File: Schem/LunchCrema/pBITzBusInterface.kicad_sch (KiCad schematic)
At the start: 1 part, among them J1 pBITzBus

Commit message: Added wait state generator to LaunchCrema
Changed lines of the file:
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@@
+	)
+	(junction
+		(at 146.05 173.99)
+		(diameter 0)
+		(color 0 0 0 0)
 	)
 	(junction
@@
 	(wire
 		(pts
+			(xy 146.05 173.99) (xy 149.86 173.99)
+		)
+		(stroke
+			(width 0)
+			(type default)
+		)
+	)
+	(wire
+		(pts
 			(xy 262.89 185.42) (xy 274.32 185.42)
 		)
@@
 		(effects
 			(font
+				(size 1.27 1.27)
+			)
+			(justify left)
+		)
+	)
+	(hierarchical_label "D1"
+		(shape bidirectional)
+		(at 149.86 173.99 0)
+		(effects
+			(font

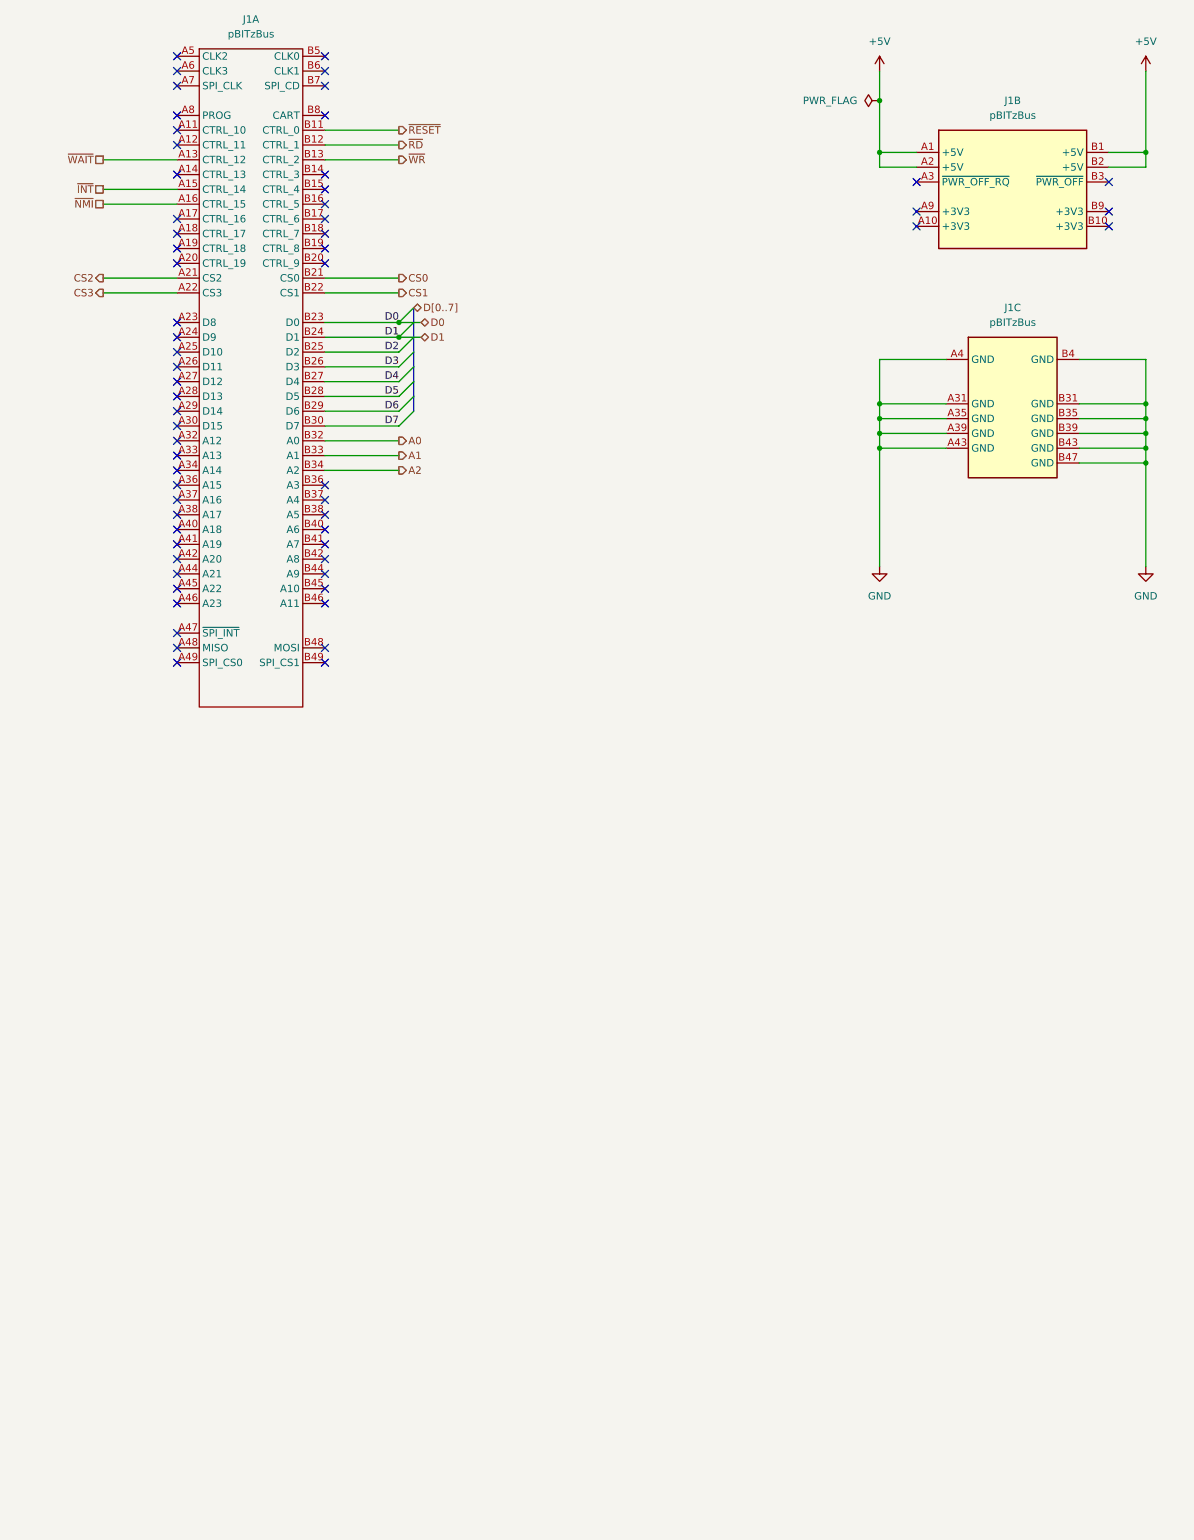
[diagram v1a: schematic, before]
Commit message: Moved to the DIN Connector
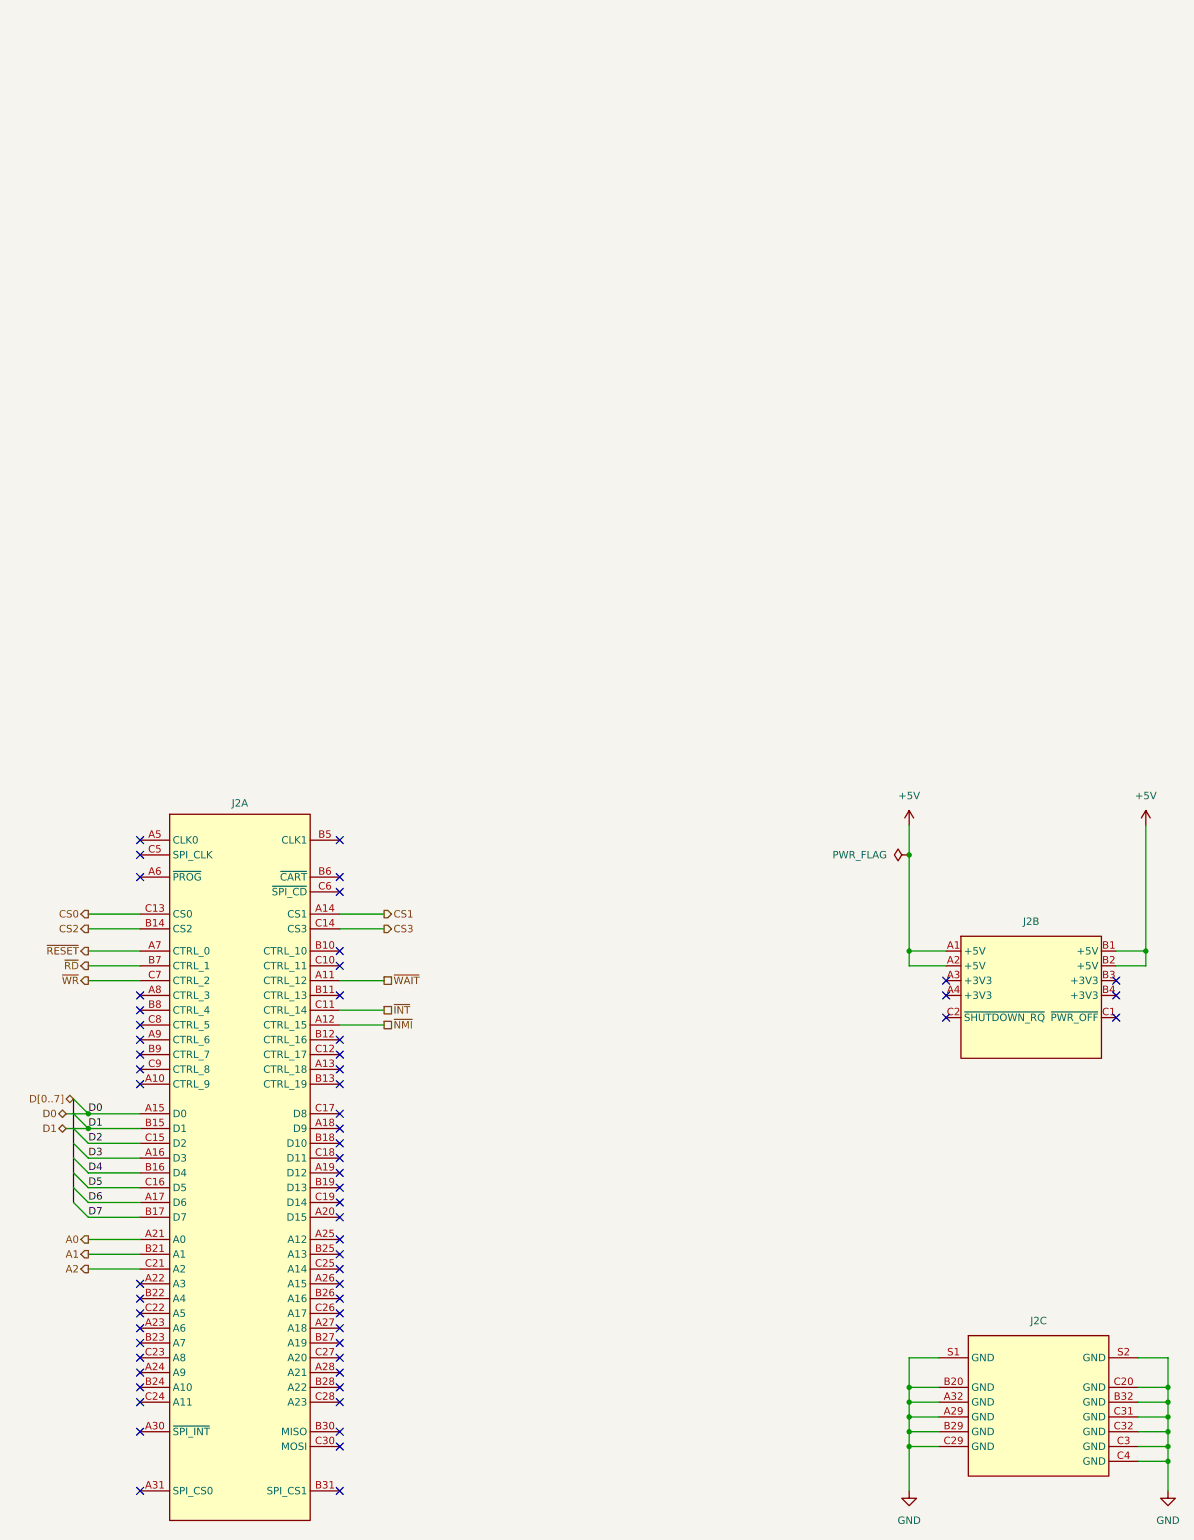
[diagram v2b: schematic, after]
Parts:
- removed J1: pBITzBus, Connector_PCBEdge:BUS_PCIexpress_x8, symbol pBITz:pBITzBus
- added J2: (no value), Footprints:AMPHENOL_86093967113T55F1LF, symbol pBITz:pBITzBus_DIN
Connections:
- net +5V: now also J2.A1 (+5V), J2.A2 (+5V), J2.B1 (+5V), J2.B2 (+5V)
- net A0: now also J2.A21 (A0)
- net A1: now also J2.B21 (A1)
- net A2: now also J2.C21 (A2)
- net CS0: now also J2.C13 (CS0)
- net CS1: now also J2.A14 (CS1)
- net CS2: now also J2.B14 (CS2)
- net CS3: now also J2.C14 (CS3)
- net D0: now also J2.A15 (D0)
- net D1: now also J2.B15 (D1)
- net D2: now also J2.C15 (D2)
- net D3: now also J2.A16 (D3)
- net D4: now also J2.B16 (D4)
- net D5: now also J2.C16 (D5)
- net D6: now also J2.A17 (D6)
- net D7: now also J2.B17 (D7)
- net GND: now also J2.A29 (GND), J2.A32 (GND), J2.B20 (GND), J2.B29 (GND), J2.B32 (GND), J2.C20 (GND), J2.C29 (GND), J2.C3 (GND), J2.C31 (GND), J2.C32 (GND), J2.C4 (GND), J2.S1 (GND), J2.S2 (GND)
- net ~{INT}: now also J2.C11 (CTRL_14)
- net ~{NMI}: now also J2.A12 (CTRL_15)
- net ~{RD}: now also J2.B7 (CTRL_1)
- net ~{RESET}: now also J2.A7 (CTRL_0)
- net ~{WAIT}: now also J2.A11 (CTRL_12)
- net ~{WR}: now also J2.C7 (CTRL_2)
- no-connect marks 62 -> 60

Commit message: updated the part #s
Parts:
- J2: MANUFACTURER_PART_NUMBER (none) -> 86093967113T55F1LF
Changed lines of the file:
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@@
+			)
+		)
+		(property "MANUFACTURER_PART_NUMBER" "86093967113T55F1LF"
+			(at 118.745 254 0)
+			(hide yes)
+			(show_name no)
+			(do_not_autoplace no)
+			(effects
+				(font
+					(size 1.27 1.27)
+				)
 			)
 		)
@@
 			)
 		)
+		(property "MANUFACTURER_PART_NUMBER" "86093967113T55F1LF"
+			(at 254.635 275.59 0)
+			(hide yes)
+			(show_name no)
+			(do_not_autoplace no)
+			(effects
+				(font
+					(size 1.27 1.27)
+				)
+			)
+		)
 		(pin "B26"
 		)
@@
 			(at 255.905 342.9 0)
 			(hide yes)
+			(show_name no)
+			(do_not_autoplace no)
+			(effects
+				(font
+					(size 1.27 1.27)
+				)
+			)
+		)
+		(property "MANUFACTURER_PART_NUMBER" "86093967113T55F1LF"
+			(at 255.905 342.9 0)
+			(hide yes)
